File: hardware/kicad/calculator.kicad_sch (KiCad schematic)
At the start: 23 parts, among them J1 Jack-DC, J2 AudioJack3_SwitchTR, Q1 BC547, SW37 SW_DIP_x04, U1 Pico, U2 Arduino_Nano_v2.x, U3 TFT

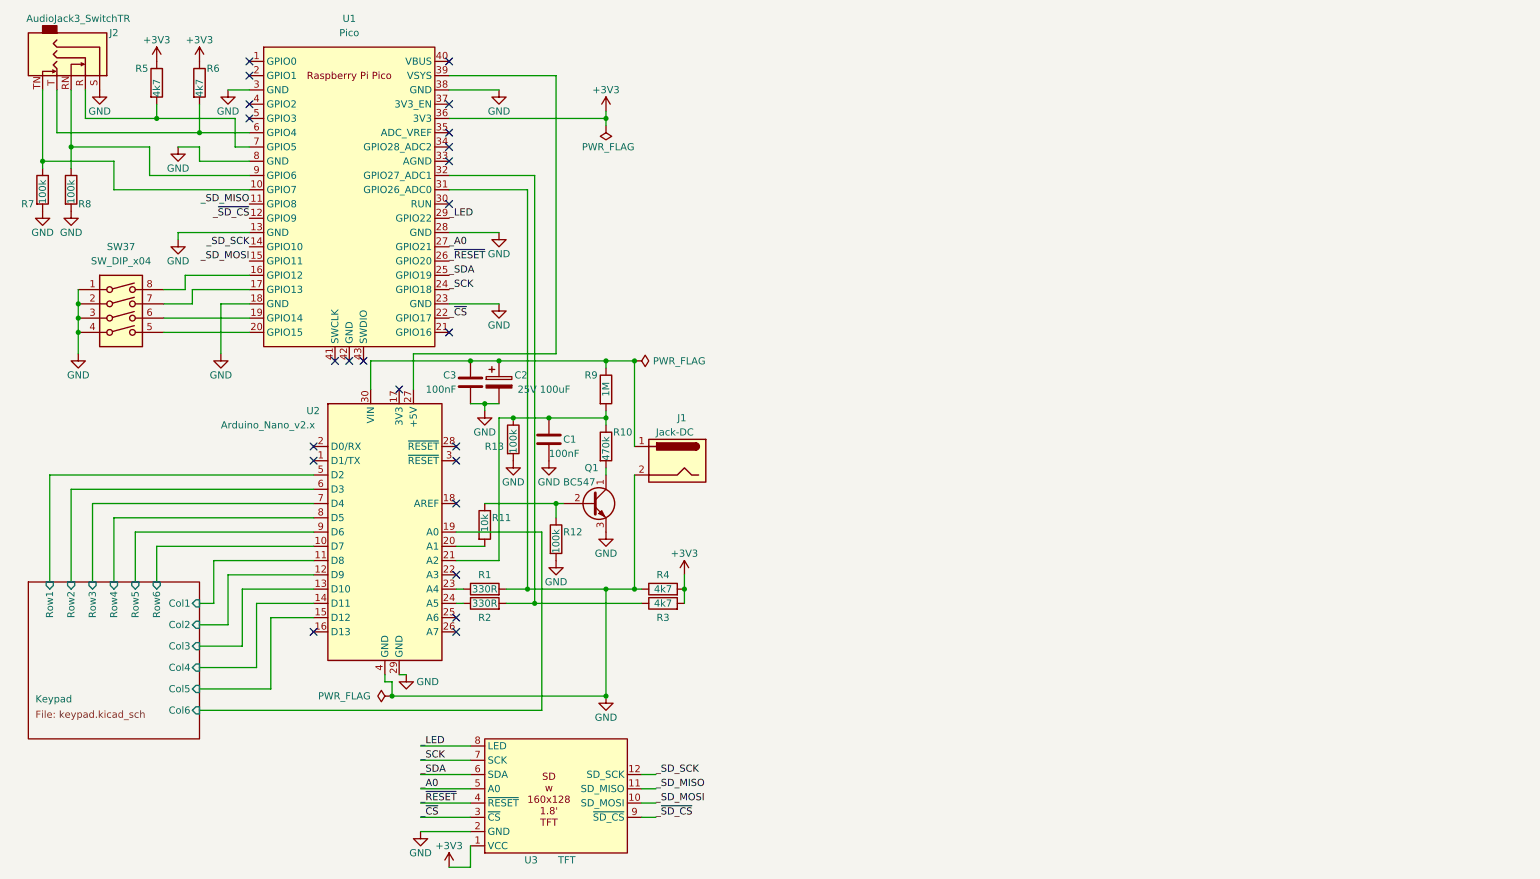
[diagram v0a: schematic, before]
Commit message: Fix: fatal error in sch & pcb (i2c bus connected to GND) 	修改：     hardware/gerber.zip 	修改：     hardware/kicad/calculator.kicad_pcb 	修改：     hardware/kicad/calculator.kicad_sch 	删除：     hardware/sch.pdf
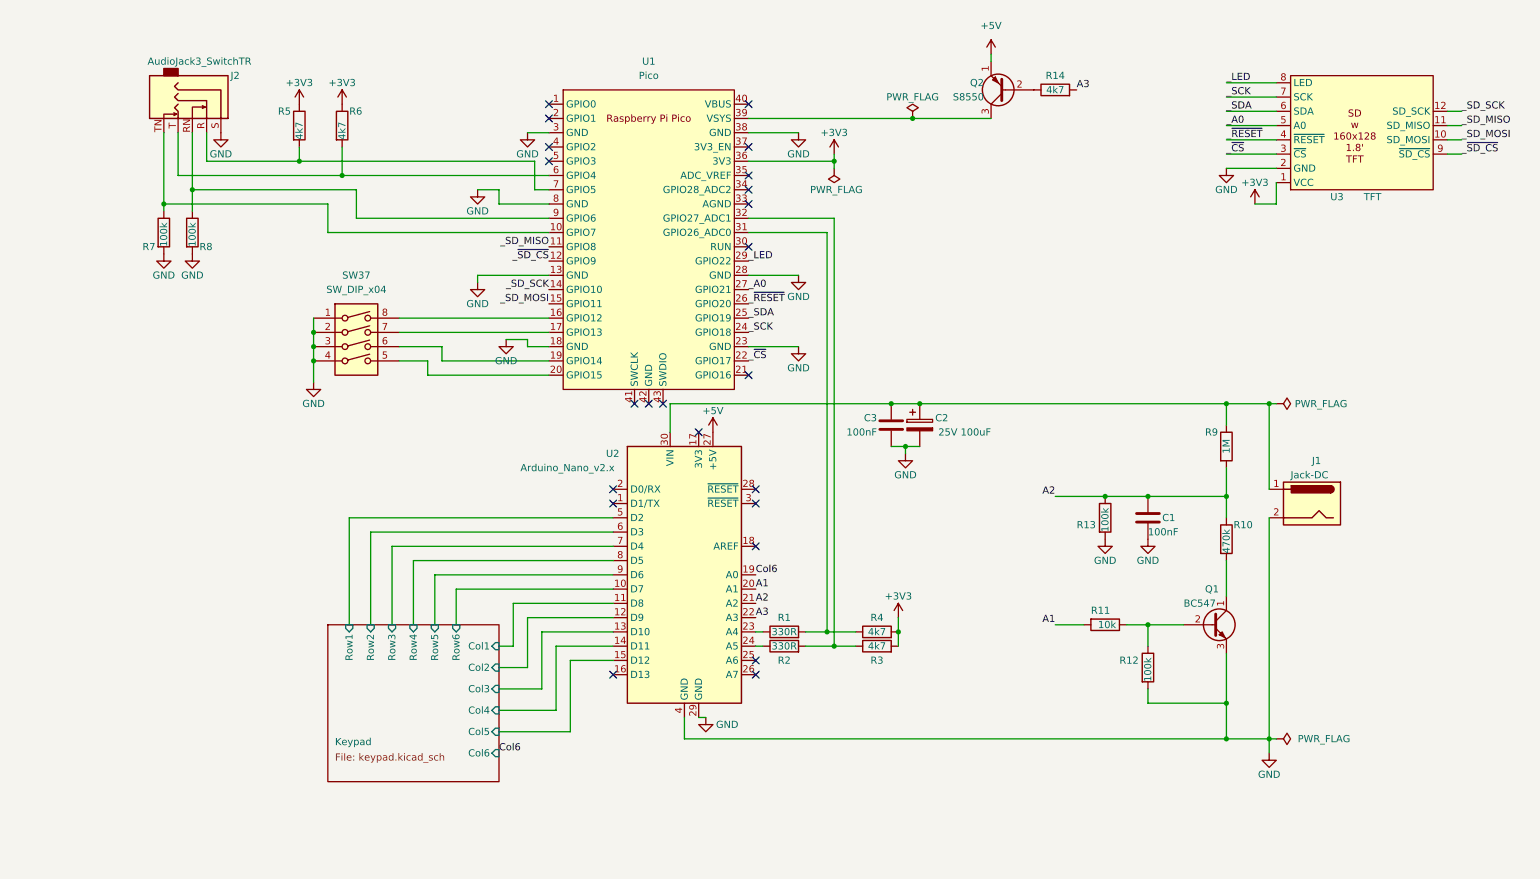
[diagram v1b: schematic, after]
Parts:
- added Q2: S8550, Package_TO_SOT_THT:TO-92_Inline, symbol Transistor_BJT:S8550
- added R14: 4k7, Resistor_THT:R_Axial_DIN0207_L6.3mm_D2.5mm_P10.16mm_Horizontal, symbol Device:R
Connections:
- net GND: no longer R1.2, R4.1, U1.31 (GPIO26_ADC0)
- net A2: now reaches C1.1, R10.1, R13.1, R9.2, U2.21 (A2)
- net A1: now reaches R11.2, U2.20 (A1)
- net A3: now reaches U2.22 (A3)
- net A3: now also R14.2
- net at U1.39 (VSYS): now also Q2.3 (C); no longer U2.27 (+5V)
- net Keypad/Col6 renamed Col6
- new net: R1.2, R4.1, U1.31 (GPIO26_ADC0)
- new net: Q2.2 (B), R14.1
- new net +5V: Q2.1 (E), U2.27 (+5V)
- no-connect marks 24 -> 23
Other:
- moved on the sheet: C1, C2, C3, J1, J2, Q1, R1, R10, R11, R12, R13, R2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
